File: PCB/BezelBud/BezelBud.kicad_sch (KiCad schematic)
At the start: 49 parts, among them J1 USB_C_Receptacle_USB2.0_14P, J2 Conn_01x05_Pin, SW1 SW_SPDT, SW2 SW_DPDT_x2, U1 USBLC6-2SC6, U2 STM32F072CBT6, U3 LP5907MFX-3.3, U4 LP5907MFX-3.3, U5 PCM1861DBT, Y1 Crystal_GND24

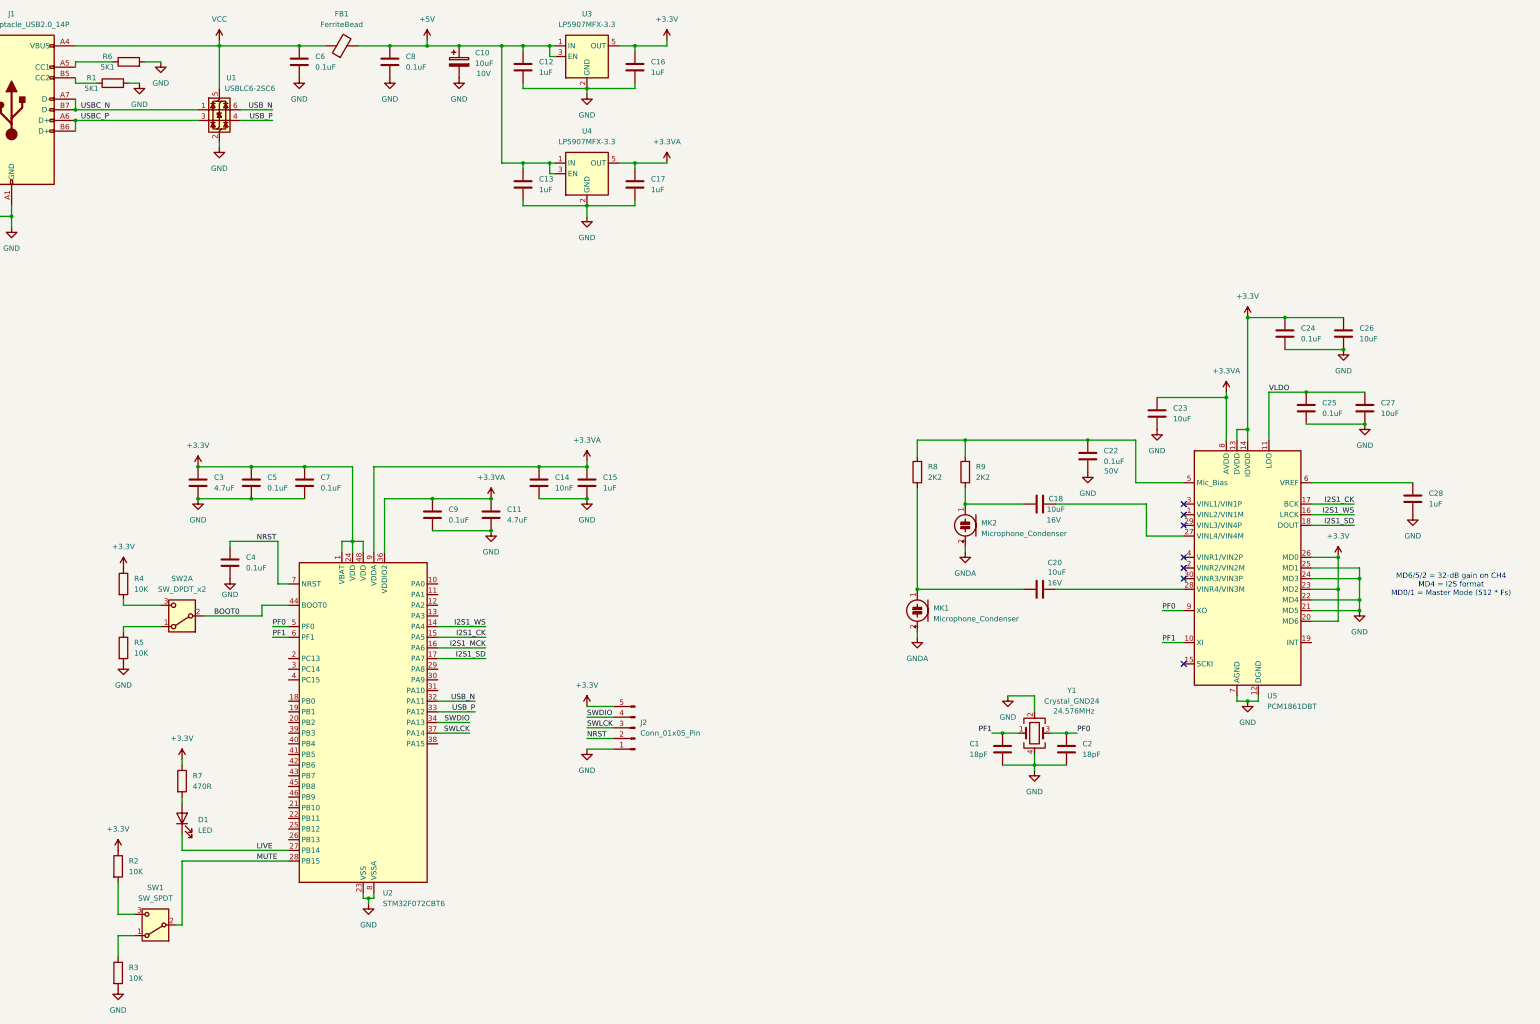
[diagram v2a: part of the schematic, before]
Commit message: Finalized component selection
Selected caps, ratings and footprints. Added crystal to codec
Added Interrupt
Wired master clk as backup
updated cubeMX to match
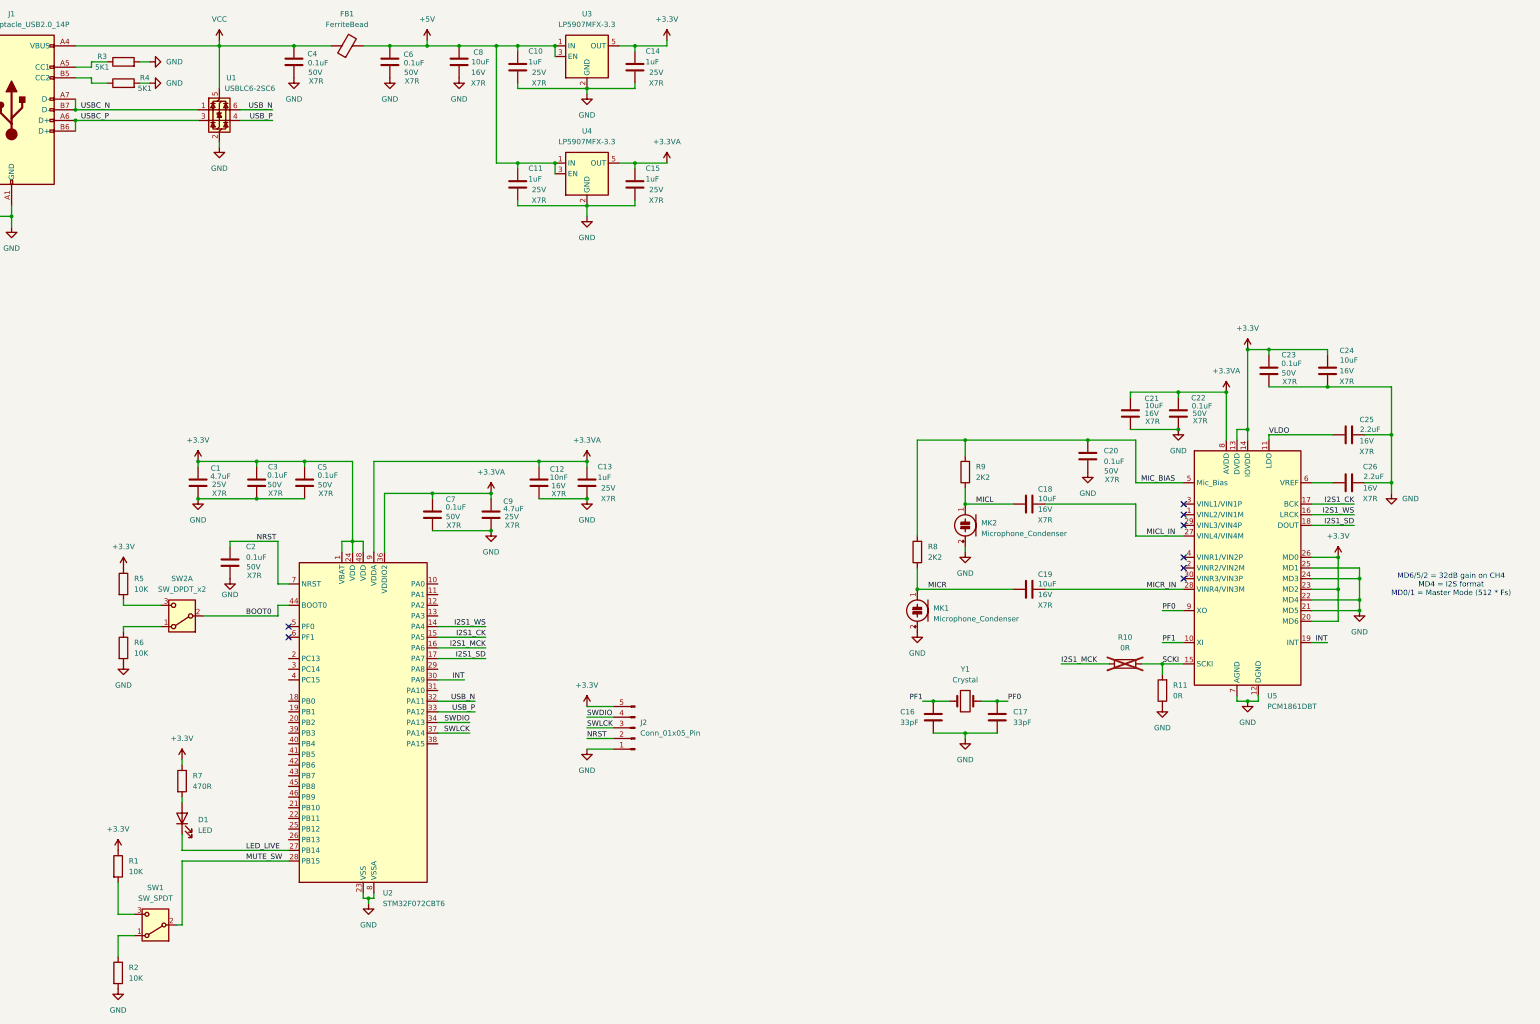
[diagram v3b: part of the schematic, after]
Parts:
- removed C10: 10uF, Capacitor_Tantalum_SMD:CP_EIA-3216-18_Kemet-A, symbol Device:C_Polarized
- removed C12, C16, C17, C28: 1uF, Capacitor_SMD:C_0603_1608Metric, symbol Device:C
- removed C20, C27: 10uF, Capacitor_SMD:C_0603_1608Metric, symbol Device:C
- removed C9: 0.1uF, Capacitor_SMD:C_0603_1608Metric, symbol Device:C
- removed Y1: Crystal_GND24, Crystal:Crystal_SMD_3225-4Pin_3.2x2.5mm, symbol Device:Crystal_GND24
- added C1: 4.7uF, Capacitor_SMD:C_0805_2012Metric, symbol Device:C
- added C10, C11, C14: 1uF, Capacitor_SMD:C_0805_2012Metric, symbol Device:C
- added C19, C21: 10uF, Capacitor_SMD:C_0805_2012Metric, symbol Device:C
- added C2, C22: 0.1uF, Capacitor_SMD:C_0603_1608Metric, symbol Device:C
- added R10, R11: 0R, Resistor_SMD:R_0603_1608Metric, symbol Device:R
- added Y1: Crystal, symbol Device:Crystal
- C12: renamed from C14; Rating (none) -> X7R; Voltage (none) -> 16V
- C13, C15: footprint Capacitor_SMD:C_0603_1608Metric -> Capacitor_SMD:C_0805_2012Metric; Rating (none) -> X7R; Voltage (none) -> 25V
- C16: renamed from C1; value 18pF -> 33pF
- C17: renamed from C2; value 18pF -> 33pF
- C18: footprint Capacitor_SMD:C_0603_1608Metric -> Capacitor_SMD:C_0805_2012Metric; Rating 16V -> X7R; Voltage (none) -> 16V
- C20: renamed from C22; Rating 50V -> X7R; Voltage (none) -> 50V
- C23: value 10uF -> 0.1uF; Rating (none) -> X7R; Voltage (none) -> 50V
- C24, C8: value 0.1uF -> 10uF; footprint Capacitor_SMD:C_0603_1608Metric -> Capacitor_SMD:C_0805_2012Metric; Rating (none) -> X7R; Voltage (none) -> 16V
- C25: value 0.1uF -> 2.2uF; Rating (none) -> X7R; Voltage (none) -> 16V
- C26: value 10uF -> 2.2uF; Rating (none) -> X7R; Voltage (none) -> 16V
- C3: value 4.7uF -> 0.1uF; Rating (none) -> X7R; Voltage (none) -> 50V
- C4, C5, C6, C7: Rating (none) -> X7R; Voltage (none) -> 50V
- C9: renamed from C11; footprint Capacitor_SMD:C_0603_1608Metric -> Capacitor_SMD:C_0805_2012Metric; Rating (none) -> X7R; Voltage (none) -> 25V
- renumbered R2 to R1, R3 to R2, R6 to R3, R1 to R4, R4 to R5, R5 to R6
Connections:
- net GNDA is gone; now on net GND: MK1.2 (+), MK2.2 (+)
- net +3.3V: now also C23.1, C1.1, C14.1; no longer C26.1, C7.1
- net +3.3VA: now also C13.1, C7.1, C21.1, C22.1; no longer C23.1
- net +5V: now also C6.1, C10.1, C11.1; no longer C13.1
- net GND: now also C1.2, C10.2, C11.2, C14.2, C2.2, C21.2, C22.2, R11.1
- net I2S1_MCK: now also R10.1
- net NRST: now also C2.1; no longer C4.1
- net PF0: now also Y1.2; no longer U2.5 (PF0)
- net PF1: now also Y1.1; no longer U2.6 (PF1)
- net VCC: now also C4.1; no longer C6.1
- net MICL: now reaches C18.1, MK2.1 (-), R9.1
- net MIC_BIAS: now reaches C20.1, R8.2, R9.2, U5.5 (Mic_Bias)
- net MICR: now reaches MK1.1 (-), R8.1
- net MICR: now also C19.1
- net MICR_IN: now reaches U5.28 (VINR4/VIN3M)
- net MICR_IN: now also C19.2
- net at U5.6 (VREF): now also C26.1
- net SCKI: now reaches U5.15 (SCKI)
- net SCKI: now also R10.2, R11.2
- net INT: now reaches U5.19 (INT)
- net INT: now also U2.30 (PA9)
- net MICL_IN: now reaches C18.2, U5.27 (VINL4/VIN4M)
- net LIVE renamed LED_LIVE
- net MUTE renamed MUTE_SW
- no-connect marks 7 -> 8
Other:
- note added: "MD6/5/2 = 32dB gain on CH4 MD4 = I2S format MD0/1 = Master Mode (512 * Fs)"
- note removed: "MD6/5/2 = 32-dB gain on CH4 MD4 = I2S format MD0/1 = Master Mode (512 * Fs)"
- moved on the sheet: C16, C17, FB1, R3, R4, R8

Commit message: Added Footprint for Crystal and Microphone
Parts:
- MK1, MK2: footprint (none) -> Sensor_Audio:POM-2244P-C3310-2-R
- Y1: footprint (none) -> Crystal:Crystal_SMD_HC49-SD
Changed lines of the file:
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@@
 			)
 		)
-		(property "Footprint" ""
+		(property "Footprint" "Sensor_Audio:POM-2244P-C3310-2-R"
 			(at 257.81 143.51 90)
 			(effects
@@
 			)
 		)
-		(property "Footprint" ""
+		(property "Footprint" "Sensor_Audio:POM-2244P-C3310-2-R"
 			(at 246.38 163.83 90)
 			(effects
@@
 			)
 		)
-		(property "Footprint" ""
+		(property "Footprint" "Crystal:Crystal_SMD_HC49-SD"
 			(at 257.81 182.88 0)
 			(effects

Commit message: Numerous quality of life changes and started PCB Design
- Configuration pins
- 16P USBC
- Removed Microphone pads, will be using a small 2 pin pad for now
- reduced part count if possible
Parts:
- removed J1: USB_C_Receptacle_USB2.0_14P, symbol Connector:USB_C_Receptacle_USB2.0_14P
- removed R2: 10K, Resistor_SMD:R_0603_1608Metric, symbol Device:R
- removed SW2: SW_DPDT_x2, Connector_PinHeader_2.54mm:PinHeader_1x03_P2.54mm_Vertical, symbol Switch:SW_DPDT_x2
- removed Y1: Crystal, Crystal:Crystal_SMD_HC49-SD, symbol Device:Crystal
- added D2: LED, LED_SMD:LED_0603_1608Metric, symbol Device:LED
- added H1, H2, H3, H4: MountingHole, MountingHole:MountingHole_3.2mm_M3_Pad_Via, symbol Mechanical:MountingHole
- added J1: USB_C_Receptacle_USB2.0_16P, BezelBud:CONN RCPT Type-C 16POS SMD TC-005, symbol Connector:USB_C_Receptacle_USB2.0_16P
- added R11, R7, R8: 0R, Resistor_SMD:R_0603_1608Metric, symbol Device:R
- added R4: 220, Resistor_SMD:R_0603_1608Metric, symbol Device:R
- added SW2, SW3, SW4, SW5, SW6, SW7, SW8, SW9: SW_SPDT, Connector_PinHeader_2.54mm:PinHeader_1x03_P2.54mm_Vertical, symbol Switch:SW_SPDT
- added Y1: Crystal_GND24, Crystal:Crystal_SMD_3225-4Pin_3.2x2.5mm, symbol Device:Crystal_GND24
- C10: renamed from C16; value 33pF -> 18pF
- C12: renamed from C17; value 33pF -> 18pF
- D1: footprint (none) -> LED_SMD:LED_0603_1608Metric; Colour (none) -> Red
- J2: footprint (none) -> Connector_PinHeader_2.54mm:PinHeader_1x05_P2.54mm_Vertical
- R5: renamed from R7; value 470R -> 220
- R6: value 10K -> 0R
- SW1: footprint (none) -> Button_Switch_SMD:SW_SPDT_Shouhan_MSK12C02
- renumbered C6 to C11, C18 to C13, C19 to C14, C8 to C15, C20 to C16, C10 to C17, C11 to C18, C21 to C19, C22 to C20, C14 to C21, C15 to C22, C5 to C4, C7 to C5, C9 to C6, C12 to C7, C13 to C8, C4 to C9, R4 to R10, R8 to R12, R9 to R13, R10 to R14, R11 to R15, R5 to R2, R3 to R9, U2 to U1, U1 to U2
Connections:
- net +3.3V: now also R4.1, SW3.1 (A), SW4.1 (A), SW5.1 (A), SW6.1 (A), SW7.1 (A), SW8.1 (A), SW9.1 (A); no longer U5.20 (MD6), U5.23 (MD2), U5.26 (MD0)
- net BOOT0: now also SW2.2 (B)
- net GND: now also SW1.1 (A), J1.A1 (GND), J1.A12 (GND), J1.B1 (GND), J1.B12 (GND), J1.S1 (SHIELD), SW2.1 (A), SW3.3 (C), SW4.3 (C), SW5.3 (C), SW6.3 (C), SW7.3 (C), SW8.3 (C), SW9.3 (C), Y1.2 (G), Y1.4 (G); no longer R6.2, U5.21 (MD5), U5.22 (MD4), U5.24 (MD3), U5.25 (MD1)
- net I2S1_CK: now also R8.1; no longer U1.15 (PA5)
- net I2S1_MCK: now also R7.1; no longer U1.16 (PA6)
- net I2S1_SD: now also R6.1; no longer U1.17 (PA7)
- net I2S1_WS: now also R11.1; no longer U1.14 (PA4)
- net PF0: now also Y1.3
- net PF1: now also Y1.1
- net USBC_N: now also J1.A7 (D-), J1.B7 (D-)
- net USBC_P: now also J1.A6 (D+), J1.B6 (D+)
- net VCC: now also J1.A4 (VBUS), J1.A9 (VBUS), J1.B4 (VBUS), J1.B9 (VBUS)
- net CC1: now reaches R9.1
- net CC1: now also J1.A5 (CC1)
- net CC2: now reaches R10.1
- net CC2: now also J1.B5 (CC2)
- net VREF: now reaches C26.1, U5.6 (VREF)
- net SW_H: now reaches R1.2, SW1.3 (C)
- net at R5.2: now also D2.2 (A); no longer D1.2 (A)
- net BOOT_H: now reaches R2.2
- net BOOT_H: now also SW2.3 (C)
- net LED_BLINK: now reaches U1.26 (PB13)
- net LED_BLINK: now also D2.1 (K)
- net MIC_BIAS renamed BIAS
- new net: D1.2 (A), R4.2
- new net I2S1_CK_ST: R8.2, U1.15 (PA5)
- new net I2S1_MCK_ST: R7.2, U1.16 (PA6)
- new net I2S1_SD_ST: R6.2, U1.17 (PA7)
- new net I2S1_WS_ST: R11.2, U1.14 (PA4)
- new net MD0: SW6.2 (B), U5.26 (MD0)
- new net MD1: SW3.2 (B), U5.25 (MD1)
- new net MD2: SW4.2 (B), U5.23 (MD2)
- new net MD3: SW7.2 (B), U5.24 (MD3)
- new net MD4: SW8.2 (B), U5.22 (MD4)
- new net MD5: SW5.2 (B), U5.21 (MD5)
- new net MD6: SW9.2 (B), U5.20 (MD6)
- no-connect marks 8 -> 33
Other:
- note added: "Remove microphones for the board, leave solderig spot for wire. USB to be 90 degree flat"
- moved on the sheet: C1, C10, C11, C12, C13, C14, C15, C16, C17, C18, C19, C2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

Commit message: Swapped MCU to M4 need to update schematic
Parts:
- removed U1: STM32F072CBT6, Package_QFP:LQFP-48_7x7mm_P0.5mm, symbol MCU_ST_STM32F0:STM32F072CBTx
- added U6: STM32G431CBT, Package_QFP:LQFP-48_7x7mm_P0.5mm, symbol MCU_ST_STM32G4:STM32G431CBTx
- R14: now fitted
- R15: now not fitted
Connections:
- net +3.3V: now also U6.1 (VBAT), U6.24 (VDD), U6.36 (VDD)
- net +3.3VA: now also U6.21 (VDDA), U6.48 (VDD)
- net BOOT0: now also U6.7 (PG10)
- net GND: now also U6.19 (VSSA), U6.23 (VSS), U6.35 (VSS), U6.47 (VSS)
- net I2S1_CK_ST: now also U6.13 (PA5)
- net I2S1_MCK_ST: now also U6.14 (PA6)
- net I2S1_SD_ST: now also U6.15 (PA7)
- net I2S1_WS_ST: now also U6.12 (PA4)
- net INT: now also U6.31 (PA9)
- net LED_BLINK: now also U6.27 (PB13)
- net LED_LIVE: now also U6.28 (PB14)
- net MUTE_SW: now also U6.29 (PB15)
- net NRST: now also U6.20 (VREF+)
- net PF0: now also U6.5 (PF0); no longer U5.9 (XO)
- net PF1: now also U6.6 (PF1); no longer U5.10 (XI)
- net SWDIO: now also U6.37 (PA13)
- net SWLCK: now also U6.38 (PA14)
- net USB_N: now also U6.33 (PA11)
- net USB_P: now also U6.34 (PA12)
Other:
- note added: "MD6/5/2 = 32dB gain on CH4 MD4 = I2S format MD0/1 = Slave Mode Auto Detect Fs"
- note removed: "MD6/5/2 = 32dB gain on CH4 MD4 = I2S format MD0/1 = Master Mode (512 * Fs)"
- moved on the sheet: C10, C12, Y1

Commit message: small updates to schematic and layout for new stm32
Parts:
- removed C6: 4.7uF, Capacitor_SMD:C_0805_2012Metric, symbol Device:C
- removed R14, R15: 0R, Resistor_SMD:R_0603_1608Metric, symbol Device:R
- added C11, C4: 0.1uF, Capacitor_SMD:C_0603_1608Metric, symbol Device:C
- added C12: 1uF, Capacitor_SMD:C_0805_2012Metric, symbol Device:C
- C5: value 0.1uF -> 1uF; footprint Capacitor_SMD:C_0603_1608Metric -> Capacitor_SMD:C_0805_2012Metric; Voltage 50V -> 25V
- C7: value 10nF -> 0.1uF; Voltage 16V -> 50V
- C8: value 1uF -> 10nF; footprint Capacitor_SMD:C_0805_2012Metric -> Capacitor_SMD:C_0603_1608Metric; Voltage 25V -> 16V
- J1: footprint BezelBud:CONN RCPT Type-C 16POS SMD TC-005 -> Connector_USB:USB_C_Receptacle_G-Switch_GT-USB-7010ASV; Supplier (none) -> https://www.lcsc.com/product-detail/C2765186.html?s_z=n_usbc
- MICL1: renamed from MK2; footprint Sensor_Audio:POM-2244P-C3310-2-R -> Resistor_THT:R_Axial_DIN0204_L3.6mm_D1.6mm_P1.90mm_Vertical
- MICR1: renamed from MK1; footprint Sensor_Audio:POM-2244P-C3310-2-R -> Resistor_THT:R_Axial_DIN0204_L3.6mm_D1.6mm_P1.90mm_Vertical
- R3: renamed from R4; value 220 -> 1K
- R4: renamed from R5; value 220 -> 1K
- U1: renamed from U6; value STM32G431CBT -> STM32G431CBT6
- Y1: Clock (none) -> 24.576MHz
- renumbered C10 to C1, C4 to C10, C9 to C13, C11 to C14, C13 to C16, C14 to C17, C17 to C18, C18 to C19, C12 to C2, C16 to C20, C19 to C21, C21 to C22, C22 to C23, C20 to C24, C23 to C25, C24 to C26, C25 to C27, C26 to C28, C1 to C3, C2 to C6, C3 to C9, R2 to R1, R7 to R10, R12 to R11, R13 to R12, R1 to R2, R11 to R5, R8 to R6, R6 to R7, R9 to R8, R10 to R9, SW2 to SW1, SW1 to SW2
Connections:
- net SCKI is gone; now on net I2S2_MCK: U5.15 (SCKI)
- net +3.3V: now also C7.1, U1.48 (VDD), C4.1
- net +3.3VA: now also U1.20 (VREF+), C11.1, C12.1; no longer C7.1, U1.48 (VDD)
- net BOOT0: now also U1.45 (PB8); no longer U1.7 (PG10)
- net GND: now also C11.2, C12.2, C4.2
- net LED_BLINK: now also U1.16 (PB0); no longer U1.27 (PB13)
- net LED_LIVE: now also U1.17 (PB1); no longer U1.28 (PB14)
- net MUTE_SW: now also U1.18 (PB2); no longer U1.29 (PB15)
- net NRST: now also U1.7 (PG10); no longer U1.20 (VREF+)
- net I2S2_WS_ST: now reaches U1.26 (PB12)
- net I2S2_WS_ST: now also R5.1
- net I2S2_MCK_ST: now reaches U1.30 (PA8)
- net I2S2_MCK_ST: now also R10.2
- net I2S1_CK renamed I2S2_CK
- net I2S2_CK: now also R6.2; no longer R6.1
- net I2S1_CK_ST: no longer names the net of U1.13 (PA5)
- net I2S1_CK_ST: no longer R6.2
- net I2S1_MCK renamed I2S2_MCK
- net I2S1_MCK_ST: no longer names the net of U1.14 (PA6)
- net I2S1_MCK_ST: no longer R10.2
- net I2S1_SD renamed I2S2_SD
- net I2S2_SD: now also R7.2; no longer R7.1
- net I2S1_SD_ST: no longer names the net of U1.15 (PA7)
- net I2S1_SD_ST: no longer R7.2
- net I2S1_WS renamed I2S2_WS
- net I2S2_WS: now also R5.2; no longer R5.1
- net I2S1_WS_ST: no longer names the net of U1.12 (PA4)
- net I2S1_WS_ST: no longer R5.2
- new net I2S2_CK_ST: R6.1, U1.27 (PB13)
- new net I2S2_SD_ST: R7.1, U1.29 (PB15)
- no-connect marks 33 -> 32
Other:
- moved on the sheet: C1, C10, C16, C17, C2, C20, C21, C24, C25, C26, C27, C28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

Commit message: updated pcb layout
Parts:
- added C18, C20: 47uF, Capacitor_SMD:C_1206_3216Metric, symbol Device:C
- added R13: 100R, Resistor_SMD:R_0805_2012Metric, symbol Device:R
- renumbered C18 to C19, C20 to C21, C21 to C22, C19 to C23, C22 to C24, C24 to C25, C23 to C26, C25 to C27, C26 to C28, C27 to C29, C28 to C30
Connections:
- net +5V: now also R13.1; no longer C23.1, U4.1 (IN), U4.3 (EN)
- net GND: now also C18.2, C20.2
- net LED_BLINK: now also U1.41 (PB4); no longer U1.16 (PB0)
- net LED_LIVE: now also U1.42 (PB5); no longer U1.17 (PB1)
- net MUTE_SW: now also U1.43 (PB6); no longer U1.18 (PB2)
- new net +5VFIL: C18.1, C20.1, C23.1, R13.2, U4.1 (IN), U4.3 (EN)
- no-connect marks 32 -> 29
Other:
- moved on the sheet: C23, C26, R1, R2, SW1, SW2, U4
